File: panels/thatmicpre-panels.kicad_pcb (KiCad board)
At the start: 2 copper layers, 87.9 x 78 mm, 2 parts

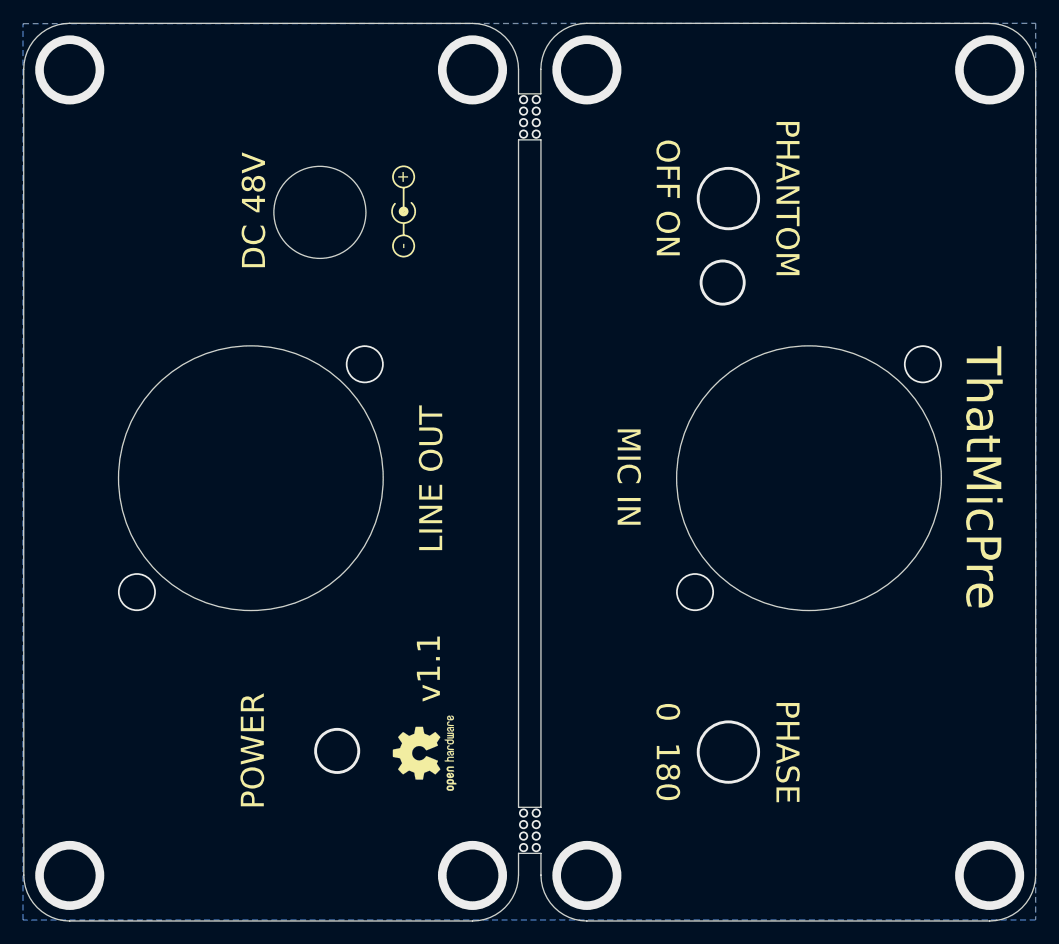
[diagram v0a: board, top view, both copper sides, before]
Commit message: Update XLR cutout radius and silkscreen placement after testfitting
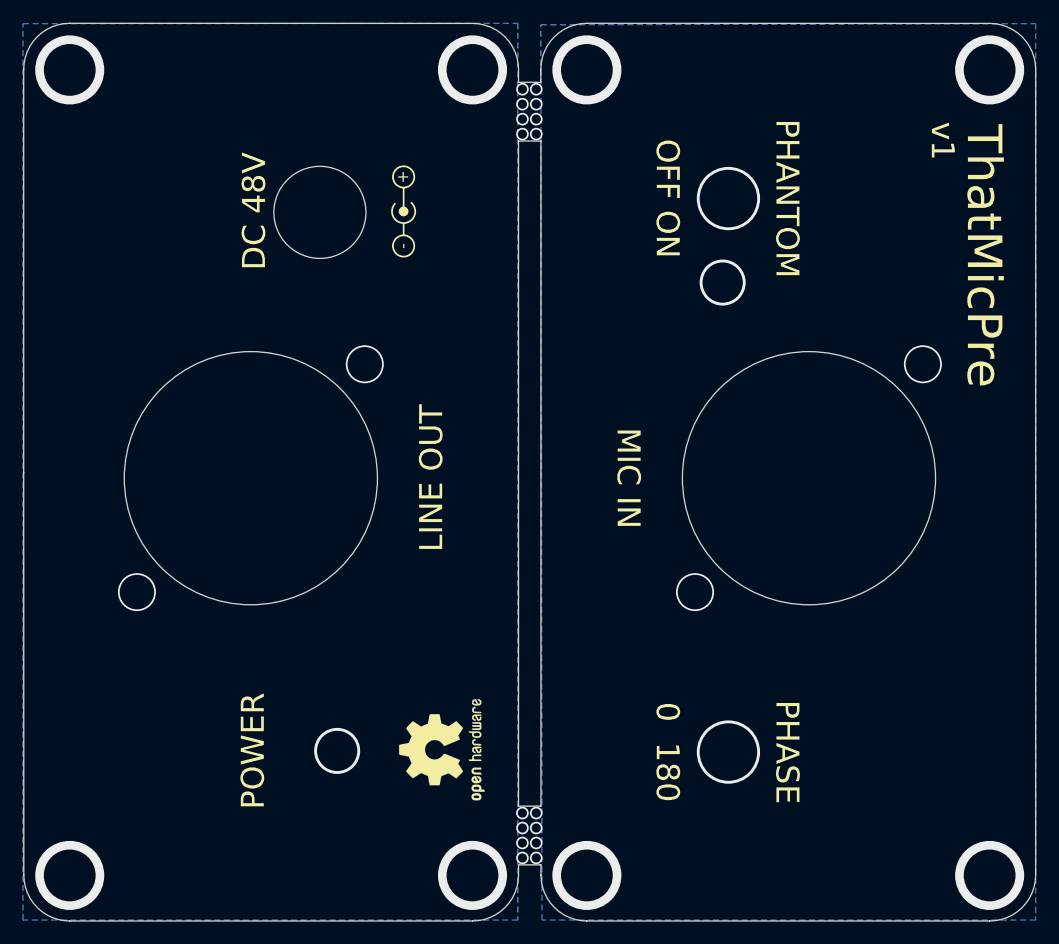
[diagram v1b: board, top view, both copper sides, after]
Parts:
- removed the REF** at (137.6, 117.9)
- added REF**: OSHW-Logo2_9.8x8mm_SilkScreen, Symbol:OSHW-Logo2_9.8x8mm_SilkScreen, F.Cu at (139.1, 117.6)
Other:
- outline, holes or cut-outs redrawn
- board text added: "v1"
- board text removed: "v1.1"
